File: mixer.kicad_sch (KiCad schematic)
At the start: 71 parts, among them T1 RF_BALUN, T2 RF_BALUN, U38 BGB741L7ESD, U4 RFFC5072, U5 FM8625H, U6 FM8625H

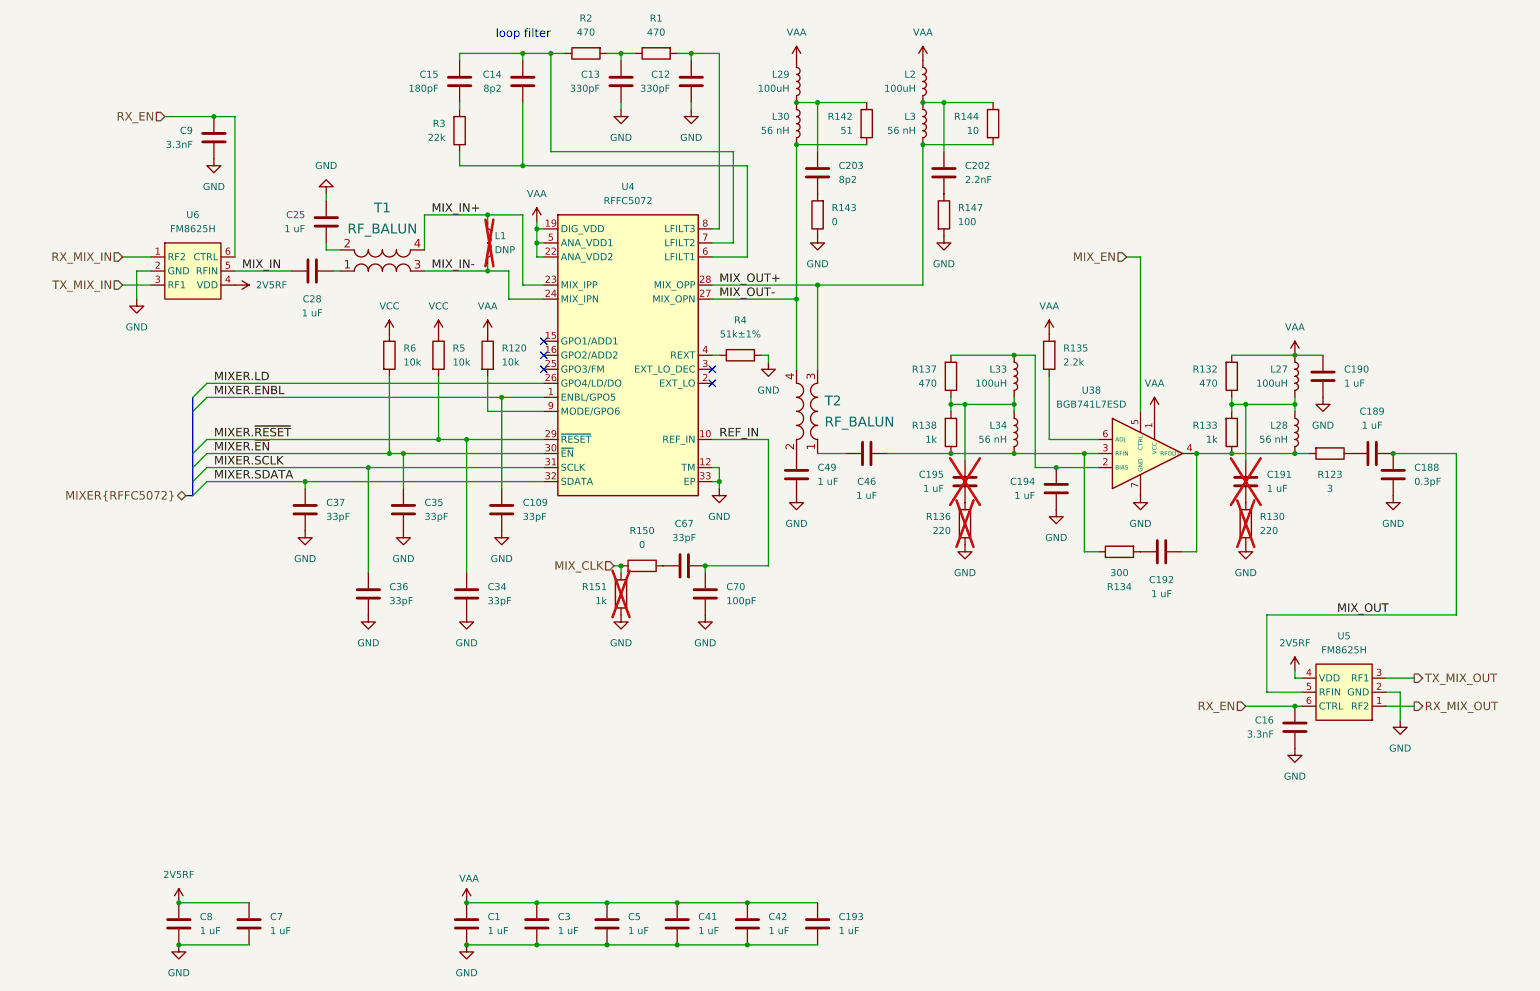
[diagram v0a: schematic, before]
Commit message: Standardize component Value fields
Use Tolerance field instead of expressing tolerance in Value field
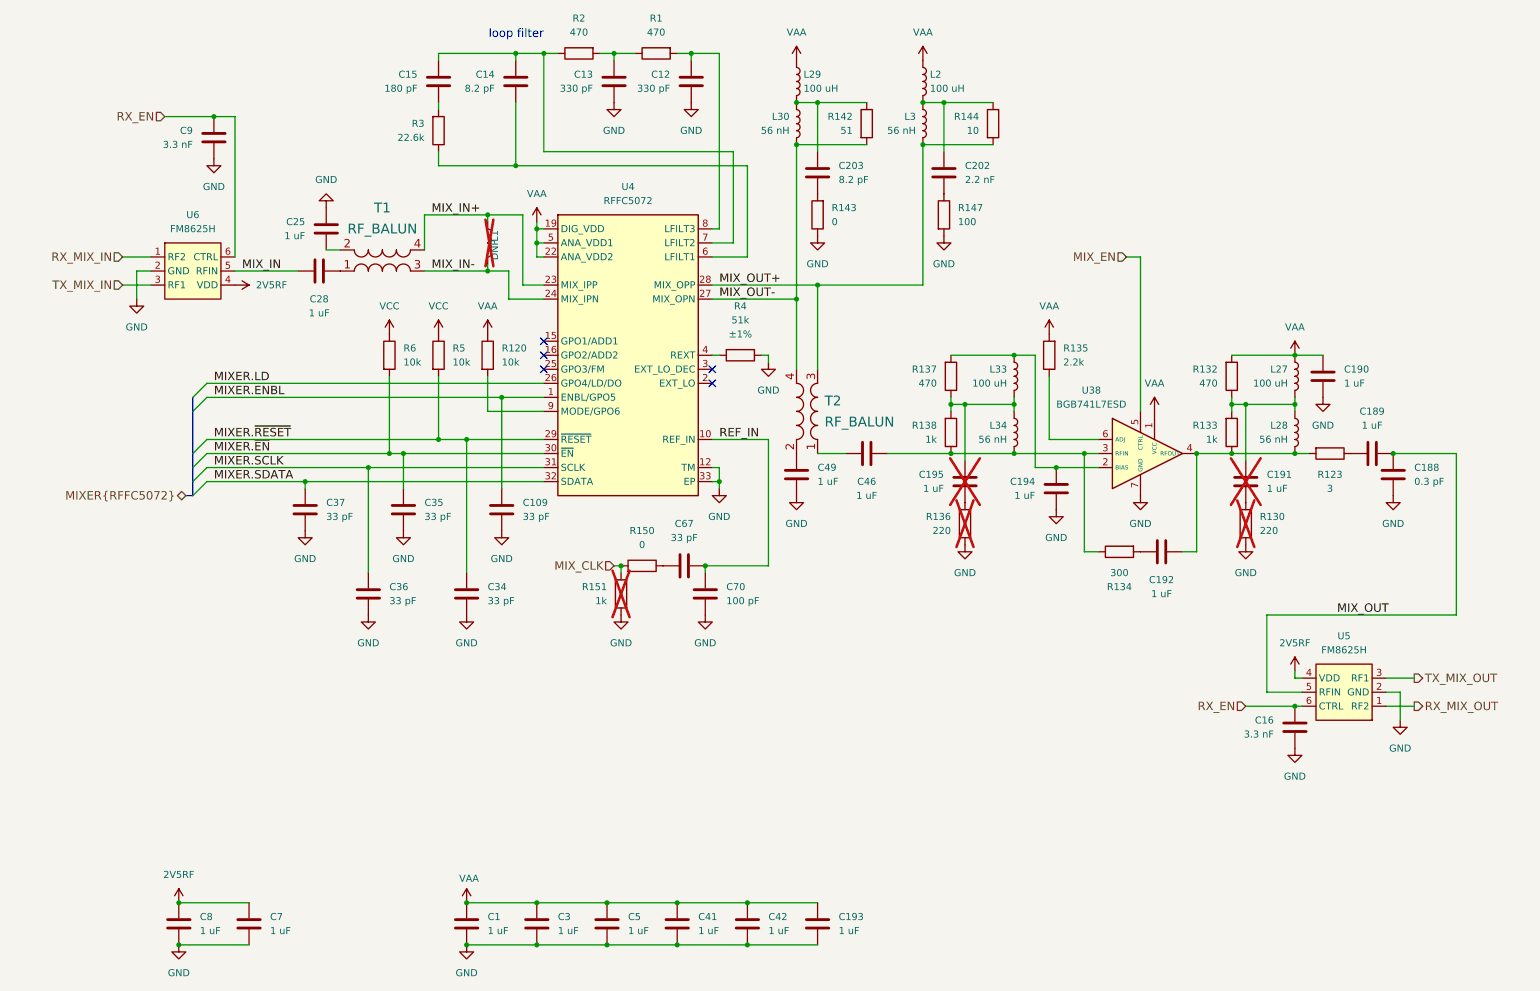
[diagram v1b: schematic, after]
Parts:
- C109, C34, C35, C36, C37, C67: value 33pF -> 33 pF
- C12, C13: value 330pF -> 330 pF
- C14, C203: value 8p2 -> 8.2 pF
- C15: value 180pF -> 180 pF
- C16, C9: value 3.3nF -> 3.3 nF
- C188: value 0.3pF -> 0.3 pF
- C202: value 2.2nF -> 2.2 nF
- C70: value 100pF -> 100 pF
- L2, L27, L29, L33: value 100uH -> 100 uH
- R3: value 22k -> 22.6k
- R4: value 51k±1% -> 51k; Tolerance (none) -> ±1%
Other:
- moved on the sheet: C13, C14, C15, C25, C28, R2, R3

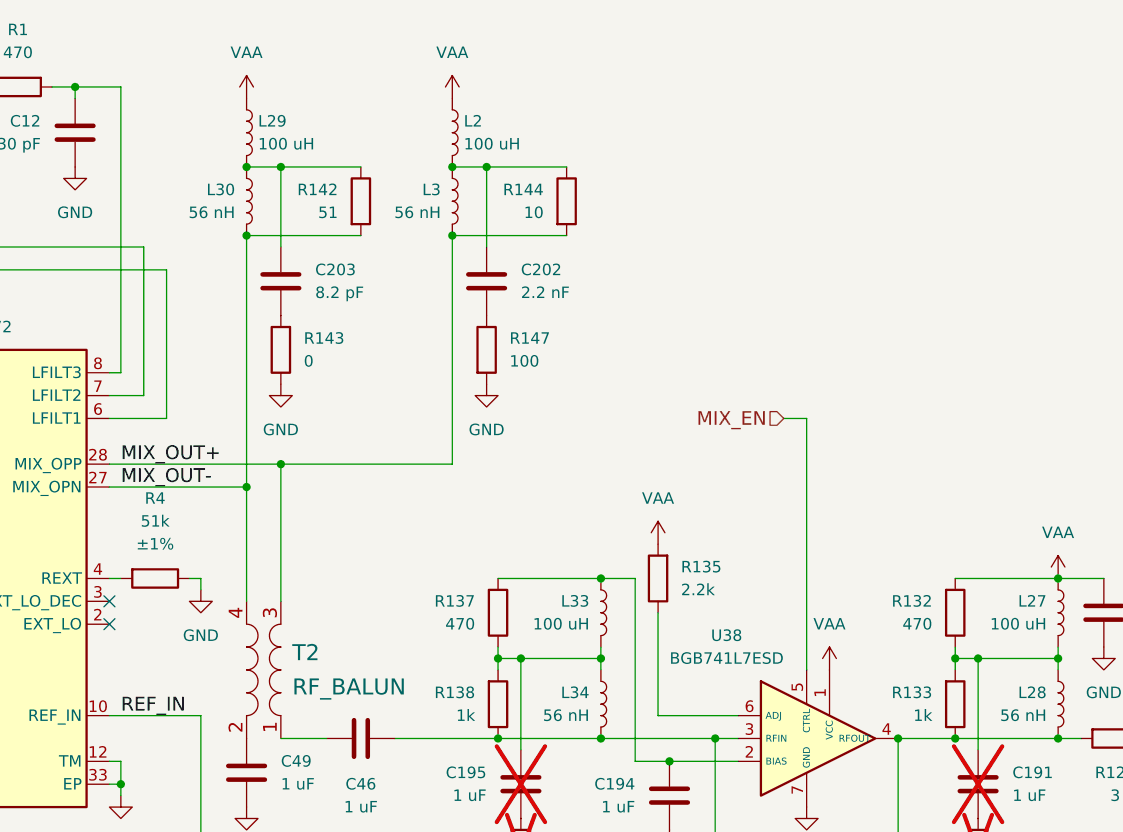
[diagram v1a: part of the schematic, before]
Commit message: Tune mixer output bias and balun
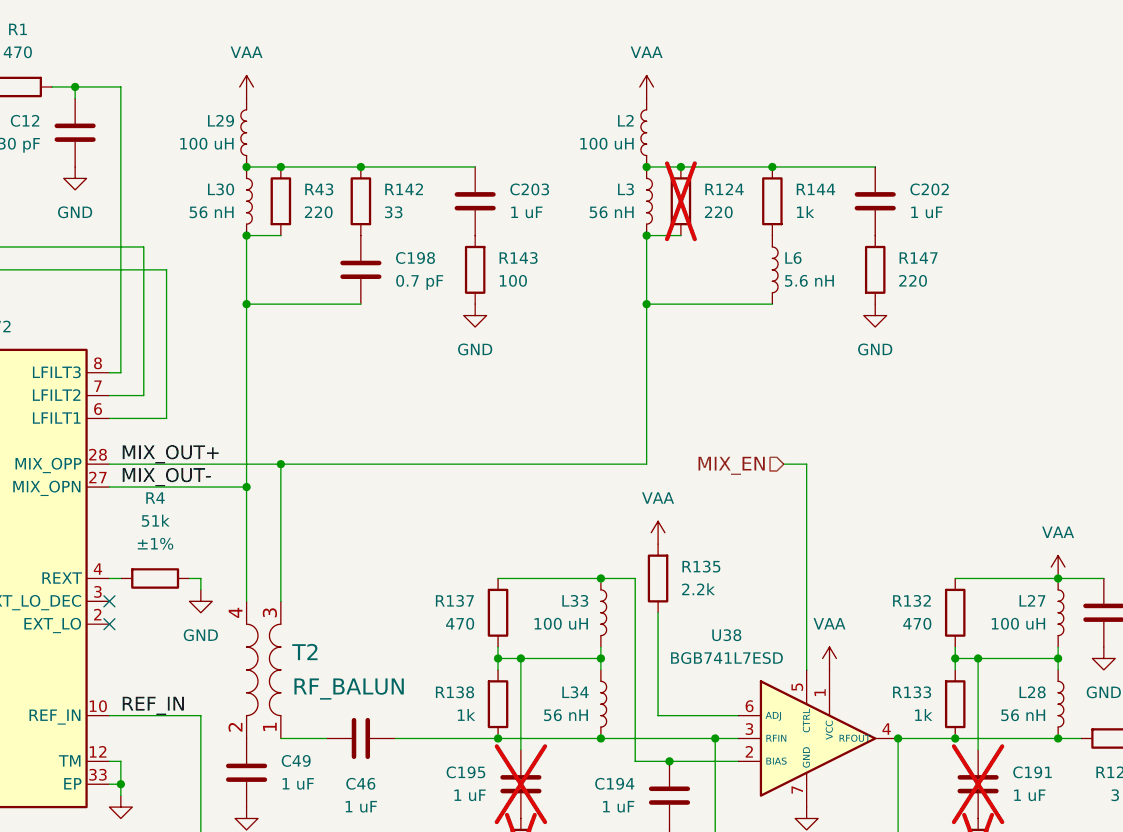
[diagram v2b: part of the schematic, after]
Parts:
- added C198: 0.7 pF, Capacitor_SMD:C_0201_0603Metric, symbol Device:C
- added L6: 5.6 nH, Inductor_SMD:L_0201_0603Metric, symbol Device:L
- added R124, R43: 220, Resistor_SMD:R_0201_0603Metric, symbol Device:R
- C202: value 2.2 nF -> 1 uF; Part Number GRM033R71A222KA01D -> GRM033R61A105ME44D
- C203: value 8.2 pF -> 1 uF; Part Number GRM0335C1H8R2CA01D -> GRM033R61A105ME44D
- R142: value 51 -> 33; Part Number RC0201JR-0751RL -> RC0201JR-0733RL
- R143: value 0 -> 100; Part Number RC0201JR-070RL -> RC0201JR-07100RL
- R144: value 10 -> 1k; Part Number RC0201JR-0710RL -> RC0201FR-071KL
- R147: value 100 -> 220; Part Number RC0201JR-07100RL -> RC0201JR-07220RL
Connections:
- net MIX_OUT+: now also L6.2, R124.2; no longer R144.2
- net MIX_OUT-: now also C198.1, R43.2; no longer R142.2
- net at C203.1, L29.2, L30.1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: now also R43.1
- net at C202.2, L2.2, L3.1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: now also R124.1
- new net: L6.1, R144.2
- new net: C198.2, R142.2
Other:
- moved on the sheet: C202, C203, L2, L29, L3, R143, R144, R147

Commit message: Update U4 pull-ups
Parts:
- removed R6: 10k, Resistor_SMD:R_0402_1005Metric, symbol Device:R
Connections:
- net VCC is gone; now on net VAA: R5.1
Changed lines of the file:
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@@
 	)
 	(junction
-		(at 78.74 99.06)
-		(diameter 0)
-		(color 0 0 0 0)
-	)
-	(junction
 		(at 260.35 99.06)
 		(diameter 0)
@@
 	(wire
 		(pts
-			(xy 78.74 85.09) (xy 78.74 99.06)
-		)
-		(stroke
-			(width 0)
-			(type default)
-		)
-	)
-	(wire
-		(pts
 			(xy 196.85 43.18) (xy 196.85 50.8)
 		)
@@
 	(wire
 		(pts
-			(xy 78.74 99.06) (xy 81.28 99.06)
-		)
-		(stroke
-			(width 0)
-			(type default)
-		)
-	)
-	(wire
-		(pts
 			(xy 196.85 50.8) (xy 196.85 68.58)
 		)
@@
 	(wire
 		(pts
-			(xy 45.72 99.06) (xy 78.74 99.06)
+			(xy 45.72 99.06) (xy 81.28 99.06)
 		)
 		(stroke
@@
 	)
 	(symbol
+		(lib_id "power:VAA")
+		(at 87.63 77.47 0)
+		(unit 1)
+		(exclude_from_sim no)
+		(in_bom yes)
+		(on_board yes)
+		(dnp no)
+		(fields_autoplaced yes)
+		(property "Reference" "#PWR055"
+			(at 87.63 81.28 0)
+			(effects
+				(font
+					(size 1.27 1.27)
+				)
+				(hide yes)
+			)
+		)
+		(property "Value" "VAA"
+			(at 87.63 72.39 0)
+			(effects
+				(font
+					(size 1.27 1.27)
+				)
+			)
+		)
+		(property "Footprint" ""
+			(at 87.63 77.47 0)
+			(effects
+				(font
+					(size 1.27 1.27)
+				)
+				(hide yes)
+			)
+		)
+		(property "Datasheet" ""
+			(at 87.63 77.47 0)
+			(effects
+				(font
+					(size 1.27 1.27)
+				)
+				(hide yes)
+			)
+		)
+		(property "Description" "Power symbol creates a global label with name \"VAA\""
+			(at 87.63 77.47 0)
+			(effects
+				(font
+					(size 1.27 1.27)
+				)
+				(hide yes)
+			)
+		)
+		(pin "1"
+		)
+		(instances
+			(project "praline"
+				(path "/dba4afc6-760f-46cb-a936-032b76448f03/786d04ae-a477-4586-9df0-2e24f8eeece5"
+					(reference "#PWR055")
+					(unit 1)
+				)
+			)
+		)
+	)
+	(symbol
 		(lib_id "power:GND")
 		(at 92.71 187.96 0)
@@
 	)
 	(symbol
-		(lib_id "power:VCC")
-		(at 87.63 77.47 0)
-		(unit 1)
-		(exclude_from_sim no)
-		(in_bom yes)
-		(on_board yes)
-		(dnp no)
-		(fields_autoplaced yes)
-		(property "Reference" "#PWR062"
-			(at 87.63 81.28 0)
-			(effects
-				(font
-					(size 1.27 1.27)
-				)
-				(hide yes)
-			)
-		)
-		(property "Value" "VCC"
-			(at 87.63 72.39 0)
-			(effects
-				(font
-					(size 1.27 1.27)
-				)
-			)
-		)
-		(property "Footprint" ""
-			(at 87.63 77.47 0)
-			(effects
-				(font
-					(size 1.27 1.27)
-				)
-				(hide yes)
-			)
-		)
-		(property "Datasheet" ""
-			(at 87.63 77.47 0)
-			(effects
-				(font
-					(size 1.27 1.27)
-				)
-				(hide yes)
-			)
-		)
-		(property "Description" "Power symbol creates a global label with name \"VCC\""
-			(at 87.63 77.47 0)
-			(effects
-				(font
-					(size 1.27 1.27)
-				)
-				(hide yes)
-			)
-		)
-		(pin "1"
-		)
-		(instances
-			(project "praline"
-				(path "/dba4afc6-760f-46cb-a936-032b76448f03/786d04ae-a477-4586-9df0-2e24f8eeece5"
-					(reference "#PWR062")
-					(unit 1)
-				)
-			)
-		)
-	)
-	(symbol
 		(lib_id "praline:2V5RF")
 		(at 40.64 180.34 0)
@@
 	)
 	(symbol
-		(lib_id "Device:R")
-		(at 78.74 81.28 0)
-		(unit 1)
-		(exclude_from_sim no)
-		(in_bom yes)
-		(on_board yes)
-		(dnp no)
-		(fields_autoplaced yes)
-		(property "Reference" "R6"
-			(at 81.28 80.0099 0)
-			(effects
-				(font
-					(size 1.27 1.27)
-				)
-				(justify left)
-			)
-		)
-		(property "Value" "10k"
-			(at 81.28 82.5499 0)
-			(effects
-				(font
-					(size 1.27 1.27)
-				)
-				(justify left)
-			)
-		)
-		(property "Footprint" "Resistor_SMD:R_0402_1005Metric"
-			(at 78.74 81.28 0)
-			(effects
-				(font
-					(size 1.524 1.524)
-				)
-				(hide yes)
-			)
-		)
-		(property "Datasheet" "~"
-			(at 78.74 81.28 0)
-			(effects
-				(font
-					(size 1.524 1.524)
-				)
-				(hide yes)
-			)
-		)
-		(property "Description" "RES 10K OHM 1/16W 5% 0402 SMD"
-			(at 78.74 81.28 0)
-			(effects
-				(font
-					(size 1.524 1.524)
-				)
-				(hide yes)
-			)
-		)
-		(property "Manufacturer" "Yageo"
-			(at 78.74 81.28 0)
-			(effects
-				(font
-					(size 1.524 1.524)
-				)
-				(hide yes)
-			)
-		)
-		(property "Part Number" "RC0402JR-0710KL"
-			(at 78.74 81.28 0)
-			(effects
-				(font
-					(size 1.524 1.524)
-				)
-				(hide yes)
-			)
-		)
-		(property "Substitution" "any equivalent"
-			(at 78.74 81.28 0)
-			(effects
-				(font
-					(size 1.27 1.27)
-				)
-				(hide yes)
-			)
-		)
-		(pin "1"
-		)
-		(pin "2"
-		)
-		(instances
-			(project "praline"
-				(path "/dba4afc6-760f-46cb-a936-032b76448f03/786d04ae-a477-4586-9df0-2e24f8eeece5"
-					(reference "R6")
-					(unit 1)
-				)
-			)
-		)
-	)
-	(symbol
 		(lib_id "praline:2V5RF")
 		(at 50.8 68.58 270)
@@
 					(unit 1)
 				)
-			)
-		)
-	)
-	(symbol
-		(lib_id "power:VCC")
-		(at 78.74 77.47 0)
-		(unit 1)
-		(exclude_from_sim no)
-		(in_bom yes)
-		(on_board yes)
-		(dnp no)
-		(fields_autoplaced yes)
-		(property "Reference" "#PWR055"
-			(at 78.74 81.28 0)
-			(effects
-				(font
-					(size 1.27 1.27)
-				)
-				(hide yes)
-			)
-		)
-		(property "Value" "VCC"
-			(at 78.74 72.39 0)
-			(effects
-				(font
-					(size 1.27 1.27)
-				)
-			)
-		)
-		(property "Footprint" ""
-			(at 78.74 77.47 0)
-			(effects
-				(font
-					(size 1.27 1.27)
-				)
-				(hide yes)
-			)
-		)
-		(property "Datasheet" ""
-			(at 78.74 77.47 0)
-			(effects
-				(font
-					(size 1.27 1.27)
-				)
-				(hide yes)
-			)
-		)
-		(property "Description" "Power symbol creates a global label with name \"VCC\""
-			(at 78.74 77.47 0)
-			(effects
-				(font
-					(size 1.27 1.27)
-				)
-				(hide yes)
-			)
-		)
-		(pin "1"
-		)
-		(instances
-			(project "praline"
-				(path "/dba4afc6-760f-46cb-a936-032b76448f03/786d04ae-a477-4586-9df0-2e24f8eeece5"
-					(reference "#PWR055")
-					(unit 1)
-				)
